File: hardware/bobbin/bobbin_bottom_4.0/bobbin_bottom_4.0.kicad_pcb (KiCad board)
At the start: 2 copper layers, 90.5 x 8.5 mm, 5 parts, among them J1 OC, J2 OC, J3 IC, J4 IC

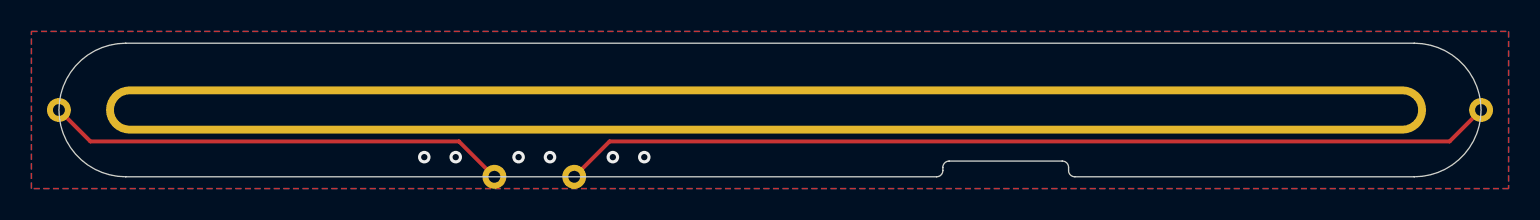
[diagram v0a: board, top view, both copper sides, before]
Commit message: adjusted for proper mouse-bites in panels
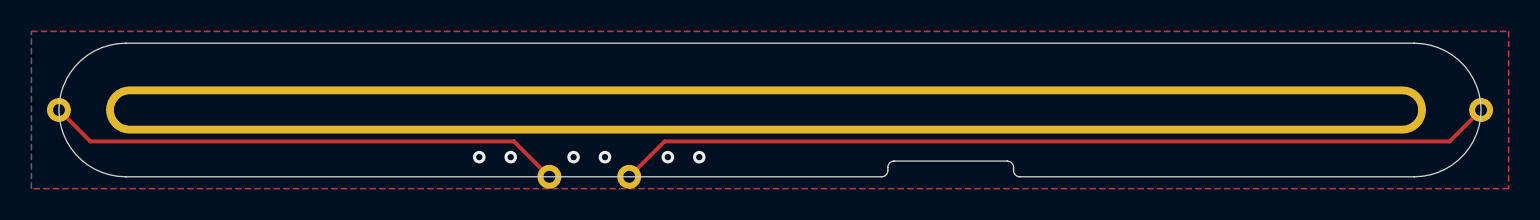
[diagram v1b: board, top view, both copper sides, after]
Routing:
- net /OC: track 59.5 -> 56.0 mm
- net /IC: track 29.5 -> 33.0 mm
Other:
- outline, holes or cut-outs redrawn
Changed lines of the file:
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@@
       (effects (font (size 1 1) (thickness 0.15)))
     )
-    (pad "1" thru_hole circle (at 0 0 180) (size 1.52 1.52) (drill 0.76) (layers *.Cu *.Mask)
+    (pad "1" thru_hole circle (at -3.5 0 180) (size 1.52 1.52) (drill 0.76) (layers *.Cu *.Mask)
       (net 2 "/OC") (pinfunction "Pin_1") (pintype "passive"))
   )
@@
       (effects (font (size 1 1) (thickness 0.15)))
     )
-    (pad "1" thru_hole circle (at 0 0) (size 1.52 1.52) (drill 0.76) (layers *.Cu *.Mask)
+    (pad "1" thru_hole circle (at 3.5 0) (size 1.52 1.52) (drill 0.76) (layers *.Cu *.Mask)
       (net 3 "/IC") (pinfunction "Pin_1") (pintype "passive"))
   )
   (gr_line (start 171 100) (end 171 102) (layer "Dwgs.User") (width 0.01))
-  (gr_arc (start 141 104.85) (mid 140.882843 105.132843) (end 140.6 105.25) (layer "Dwgs.User") (width 0.01))
-  (gr_line (start 141.4 104.25) (end 148.6 104.25) (layer "Dwgs.User") (width 0.01))
-  (gr_line (start 140.6 105.25) (end 89 105.25) (layer "Dwgs.User") (width 0.01))
-  (gr_line (start 141 104.85) (end 141 104.65) (layer "Dwgs.User") (width 0.01))
-  (gr_arc (start 111.698 105.25) (mid 112.46 104.488) (end 113.222 105.25) (layer "Dwgs.User") (width 0.01))
+  (gr_arc (start 137.5 104.85) (mid 137.382843 105.132843) (end 137.1 105.25) (layer "Dwgs.User") (width 0.01))
+  (gr_line (start 137.9 104.25) (end 145.1 104.25) (layer "Dwgs.User") (width 0.01))
+  (gr_line (start 137.1 105.25) (end 89 105.25) (layer "Dwgs.User") (width 0.01))
+  (gr_line (start 137.5 104.85) (end 137.5 104.65) (layer "Dwgs.User") (width 0.01))
+  (gr_arc (start 115.198 105.25) (mid 115.96 104.488) (end 116.722 105.25) (layer "Dwgs.User") (width 0.01))
   (gr_arc (start 89 105.25) (mid 84.75 101) (end 89 96.75) (layer "Dwgs.User") (width 0.01))
-  (gr_line (start 171 105.25) (end 149.4 105.25) (layer "Dwgs.User") (width 0.01))
+  (gr_line (start 171 105.25) (end 145.9 105.25) (layer "Dwgs.User") (width 0.01))
   (gr_arc (start 171 96.75) (mid 175.25 101) (end 171 105.25) (layer "Dwgs.User") (width 0.01))
   (gr_line (start 89 100) (end 89 102) (layer "Dwgs.User") (width 0.01))
-  (gr_line (start 149 104.65) (end 149 104.85) (layer "Dwgs.User") (width 0.01))
-  (gr_arc (start 116.778 105.25) (mid 117.54 104.488) (end 118.302 105.25) (layer "Dwgs.User") (width 0.01))
-  (gr_arc (start 149.4 105.25) (mid 149.117157 105.132843) (end 149 104.85) (layer "Dwgs.User") (width 0.01))
+  (gr_line (start 145.5 104.65) (end 145.5 104.85) (layer "Dwgs.User") (width 0.01))
+  (gr_arc (start 120.278 105.25) (mid 121.04 104.488) (end 121.802 105.25) (layer "Dwgs.User") (width 0.01))
+  (gr_arc (start 145.9 105.25) (mid 145.617157 105.132843) (end 145.5 104.85) (layer "Dwgs.User") (width 0.01))
   (gr_arc (start 175.181689 101.758932) (mid 174.488 101) (end 175.181689 100.241068) (layer "Dwgs.User") (width 0.01))
   (gr_line (start 89 100) (end 171 100) (layer "Dwgs.User") (width 0.01))
   (gr_line (start 89 96.75) (end 171 96.75) (layer "Dwgs.User") (width 0.01))
   (gr_line (start 89 102) (end 171 102) (layer "Dwgs.User") (width 0.01))
-  (gr_arc (start 141 104.65) (mid 141.117157 104.367157) (end 141.4 104.25) (layer "Dwgs.User") (width 0.01))
-  (gr_arc (start 148.6 104.25) (mid 148.882843 104.367157) (end 149 104.65) (layer "Dwgs.User") (width 0.01))
+  (gr_arc (start 137.5 104.65) (mid 137.617157 104.367157) (end 137.9 104.25) (layer "Dwgs.User") (width 0.01))
+  (gr_arc (start 145.1 104.25) (mid 145.382843 104.367157) (end 145.5 104.65) (layer "Dwgs.User") (width 0.01))
   (gr_arc (start 84.818311 100.241068) (mid 85.512 101) (end 84.818311 101.758932) (layer "Dwgs.User") (width 0.01))
-  (gr_line (start 149 104.65) (end 149 104.85) (layer "Edge.Cuts") (width 0.01))
-  (gr_arc (start 141 104.85) (mid 140.882843 105.132843) (end 140.6 105.25) (layer "Edge.Cuts") (width 0.01))
-  (gr_line (start 140.6 105.25) (end 89 105.25) (layer "Edge.Cuts") (width 0.01))
-  (gr_arc (start 149.4 105.25) (mid 149.117157 105.132843) (end 149 104.85) (layer "Edge.Cuts") (width 0.01))
-  (gr_line (start 141.4 104.25) (end 148.6 104.25) (layer "Edge.Cuts") (width 0.01))
+  (gr_line (start 145.5 104.65) (end 145.5 104.85) (layer "Edge.Cuts") (width 0.01))
+  (gr_arc (start 137.5 104.85) (mid 137.382843 105.132843) (end 137.1 105.25) (layer "Edge.Cuts") (width 0.01))
+  (gr_line (start 137.1 105.25) (end 89 105.25) (layer "Edge.Cuts") (width 0.01))
+  (gr_arc (start 145.9 105.25) (mid 145.617157 105.132843) (end 145.5 104.85) (layer "Edge.Cuts") (width 0.01))
+  (gr_line (start 137.9 104.25) (end 145.1 104.25) (layer "Edge.Cuts") (width 0.01))
   (gr_line (start 89 96.75) (end 171 96.75) (layer "Edge.Cuts") (width 0.01))
-  (gr_line (start 171 105.25) (end 149.4 105.25) (layer "Edge.Cuts") (width 0.01))
-  (gr_arc (start 141 104.65) (mid 141.117157 104.367157) (end 141.4 104.25) (layer "Edge.Cuts") (width 0.01))
-  (gr_arc (start 148.6 104.25) (mid 148.882843 104.367157) (end 149 104.65) (layer "Edge.Cuts") (width 0.01))
+  (gr_line (start 171 105.25) (end 145.9 105.25) (layer "Edge.Cuts") (width 0.01))
+  (gr_arc (start 137.5 104.65) (mid 137.617157 104.367157) (end 137.9 104.25) (layer "Edge.Cuts") (width 0.01))
+  (gr_arc (start 145.1 104.25) (mid 145.382843 104.367157) (end 145.5 104.65) (layer "Edge.Cuts") (width 0.01))
   (gr_arc (start 89 105.25) (mid 84.75 101) (end 89 96.75) (layer "Edge.Cuts") (width 0.01))
-  (gr_line (start 141 104.85) (end 141 104.65) (layer "Edge.Cuts") (width 0.01))
+  (gr_line (start 137.5 104.85) (end 137.5 104.65) (layer "Edge.Cuts") (width 0.01))
   (gr_arc (start 171 96.75) (mid 175.25 101) (end 171 105.25) (layer "Edge.Cuts") (width 0.01))
-  (via (at 120 104) (size 0.8) (drill 0.4) (layers "F.Cu" "B.Cu") (free) (net 1))
-  (via (at 122 104) (size 0.8) (drill 0.4) (layers "F.Cu" "B.Cu") (free) (net 1))
-  (via (at 116 104) (size 0.8) (drill 0.4) (layers "F.Cu" "B.Cu") (free) (net 1))
-  (via (at 108 104) (size 0.8) (drill 0.4) (layers "F.Cu" "B.Cu") (free) (net 1))
-  (via (at 110 104) (size 0.8) (drill 0.4) (layers "F.Cu" "B.Cu") (free) (net 1))
-  (via (at 114 104) (size 0.8) (drill 0.4) (layers "F.Cu" "B.Cu") (free) (net 1))
-  (segment (start 173.25 103) (end 119.79 103) (width 0.25) (layer "F.Cu") (net 2))
-  (segment (start 119.79 103) (end 117.54 105.25) (width 0.25) (layer "F.Cu") (net 2))
+  (via (at 123.5 104) (size 0.8) (drill 0.4) (layers "F.Cu" "B.Cu") (free) (net 1))
+  (via (at 125.5 104) (size 0.8) (drill 0.4) (layers "F.Cu" "B.Cu") (free) (net 1))
+  (via (at 119.5 104) (size 0.8) (drill 0.4) (layers "F.Cu" "B.Cu") (free) (net 1))
+  (via (at 111.5 104) (size 0.8) (drill 0.4) (layers "F.Cu" "B.Cu") (free) (net 1))
+  (via (at 113.5 104) (size 0.8) (drill 0.4) (layers "F.Cu" "B.Cu") (free) (net 1))
+  (via (at 117.5 104) (size 0.8) (drill 0.4) (layers "F.Cu" "B.Cu") (free) (net 1))
+  (segment (start 173.25 103) (end 123.29 103) (width 0.25) (layer "F.Cu") (net 2))
+  (segment (start 123.29 103) (end 121.04 105.25) (width 0.25) (layer "F.Cu") (net 2))
   (segment (start 175.25 101) (end 173.25 103) (width 0.25) (layer "F.Cu") (net 2))
   (segment (start 84.75 101) (end 86.75 103) (width 0.25) (layer "F.Cu") (net 3))
-  (segment (start 86.75 103) (end 110.21 103) (width 0.25) (layer "F.Cu") (net 3))
-  (segment (start 110.21 103) (end 112.46 105.25) (width 0.25) (layer "F.Cu") (net 3))
+  (segment (start 86.75 103) (end 113.71 103) (width 0.25) (layer "F.Cu") (net 3))
+  (segment (start 113.71 103) (end 115.96 105.25) (width 0.25) (layer "F.Cu") (net 3))
   (zone (net 1) (net_name "GND") (layer "F.Cu") (hatch edge 0.508)
     (connect_pads (clearance 0.25))
